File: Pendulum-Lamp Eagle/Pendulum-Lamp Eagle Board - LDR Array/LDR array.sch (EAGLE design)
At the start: 19 parts

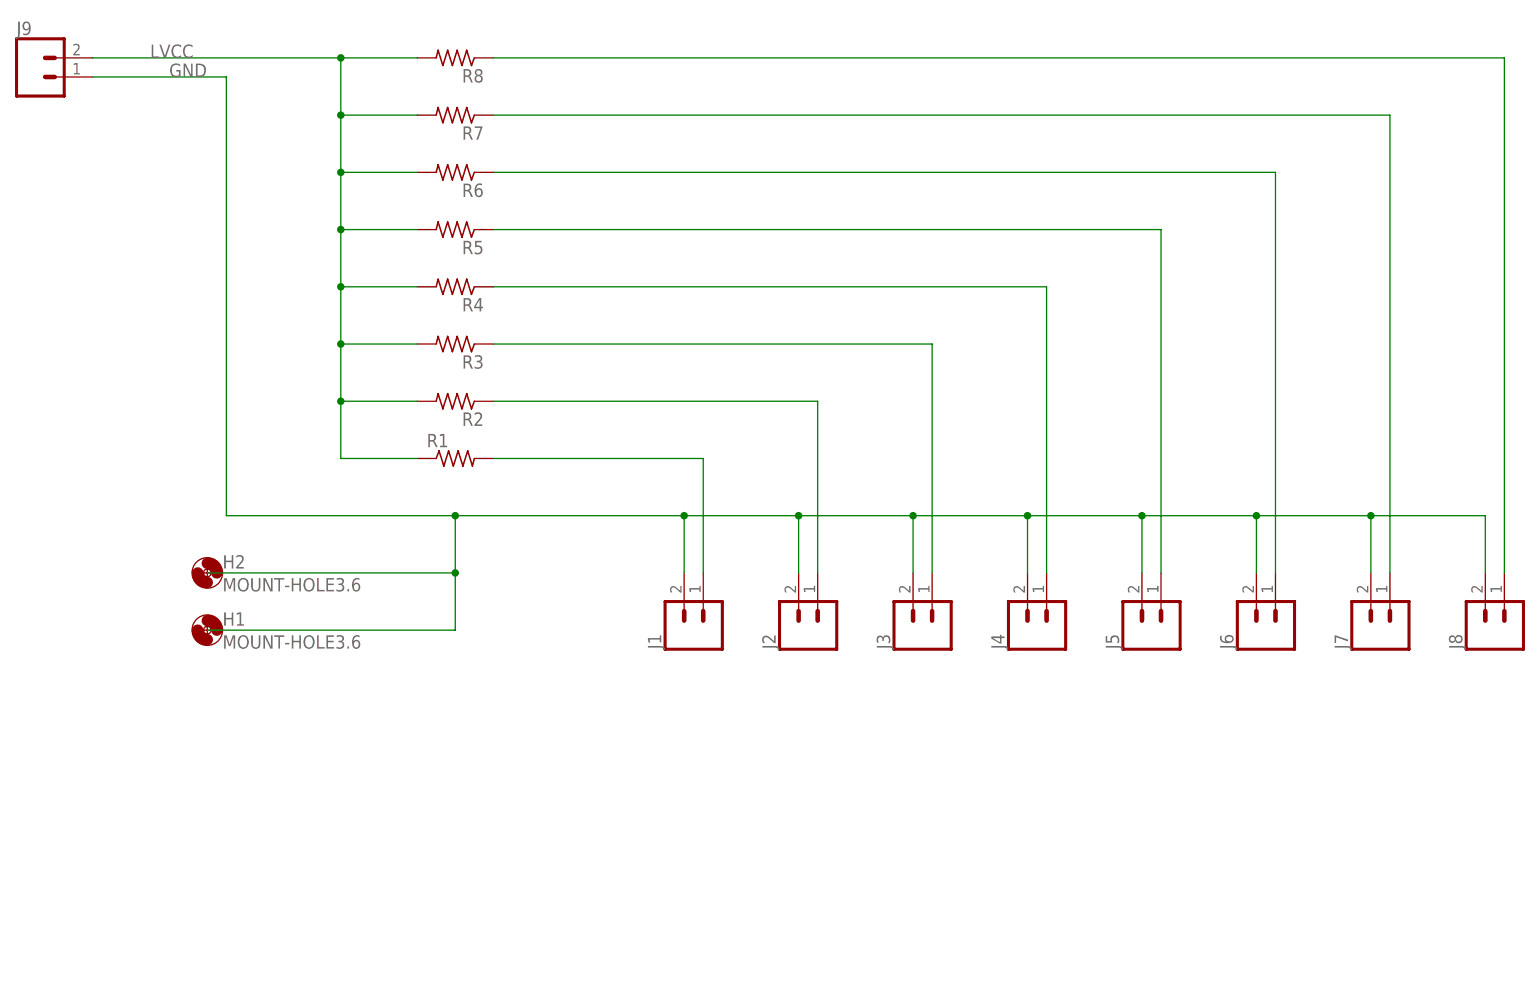
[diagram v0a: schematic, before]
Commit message: Laser array and ldr array pcb circuits designed
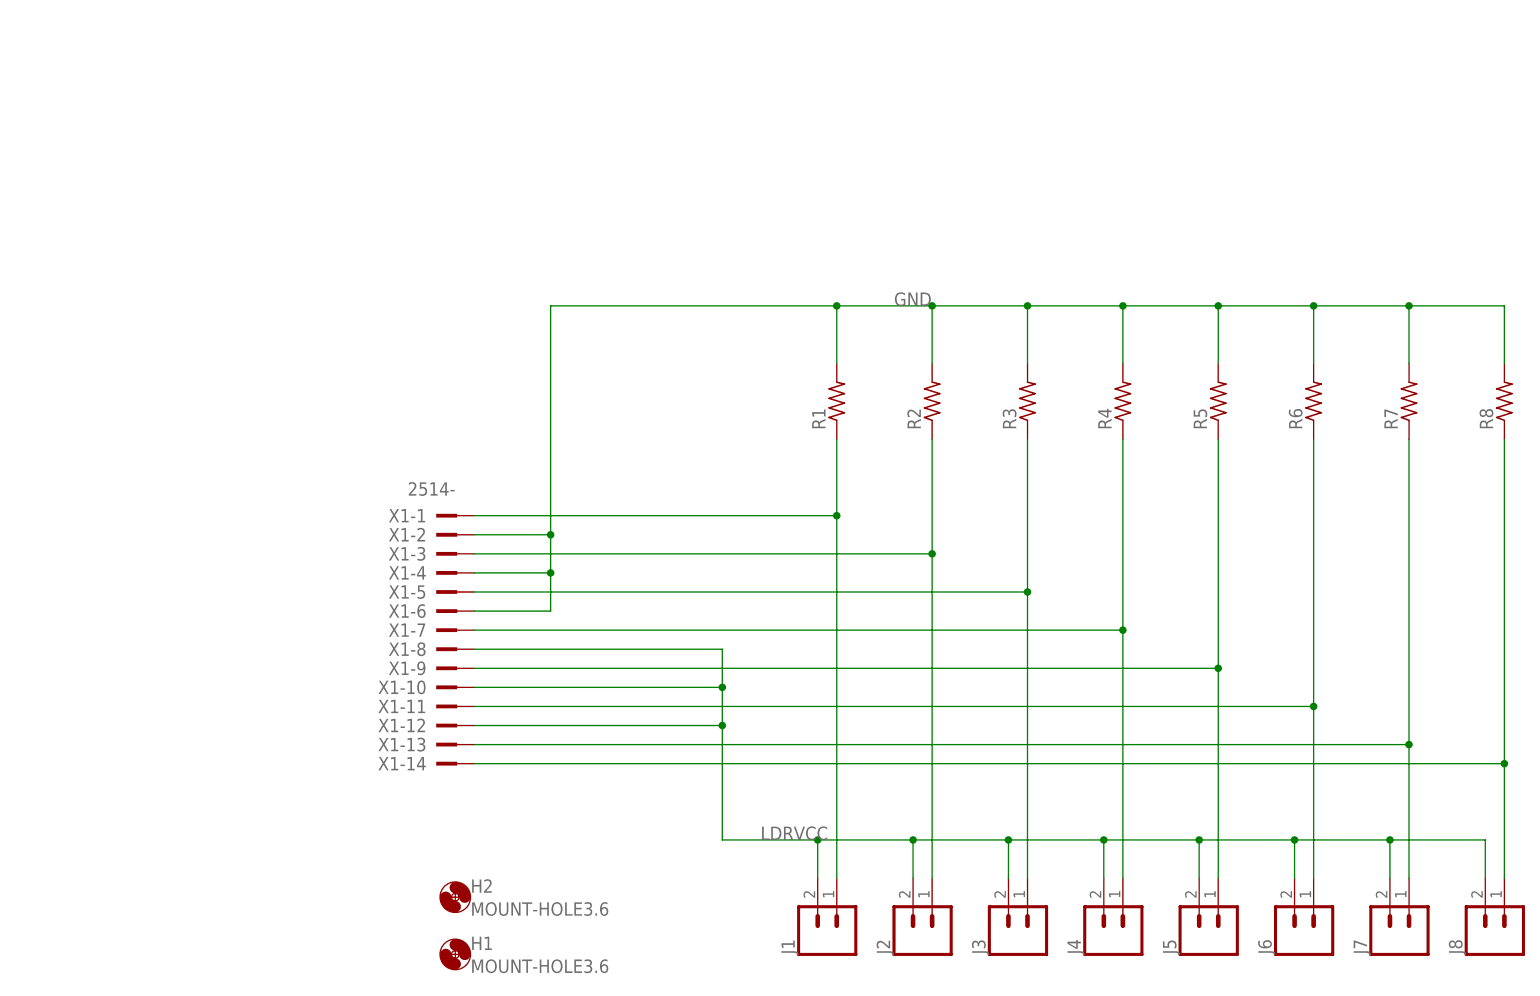
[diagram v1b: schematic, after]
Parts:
- removed J9: (no value), SparkFun-Connectors:CONN_023.5MM_LOCK
- added X1: 2514-, con-3m:2514-
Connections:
- removed net LVCC: J9.2, R1.1, R2.2, R3.2, R4.2, R5.2, R6.2, R7.2, R8.2
- new net LDRVCC: J1.2, J2.2, J3.2, J4.2, J5.2, J6.2, J7.2, J8.2, X1-10.KL, X1-12.KL, X1-8.KL
- net GND: now also R1.2, R2.2, R3.2, R4.2, R5.2, R6.2, R7.2, R8.2, X1-2.KL, X1-4.KL, X1-6.KL; no longer J1.2, J2.2, J3.2, J4.2, J5.2, J6.2, J7.2, J8.2, J9.1
- net N$1: now also R1.1, X1-1.KL; no longer R1.2
- net N$2: now also X1-3.KL
- net N$3: now also X1-5.KL
- net N$4: now also X1-7.KL
- net N$5: now also X1-9.KL
- net N$6: now also X1-11.KL
- net N$7: now also X1-13.KL
- net N$8: now also X1-14.KL
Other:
- moved on the sheet: H1, H2, J1, J2, J3, J4, J5, J6, J7, J8, R1, R2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
